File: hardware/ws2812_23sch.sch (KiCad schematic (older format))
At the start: 64 parts

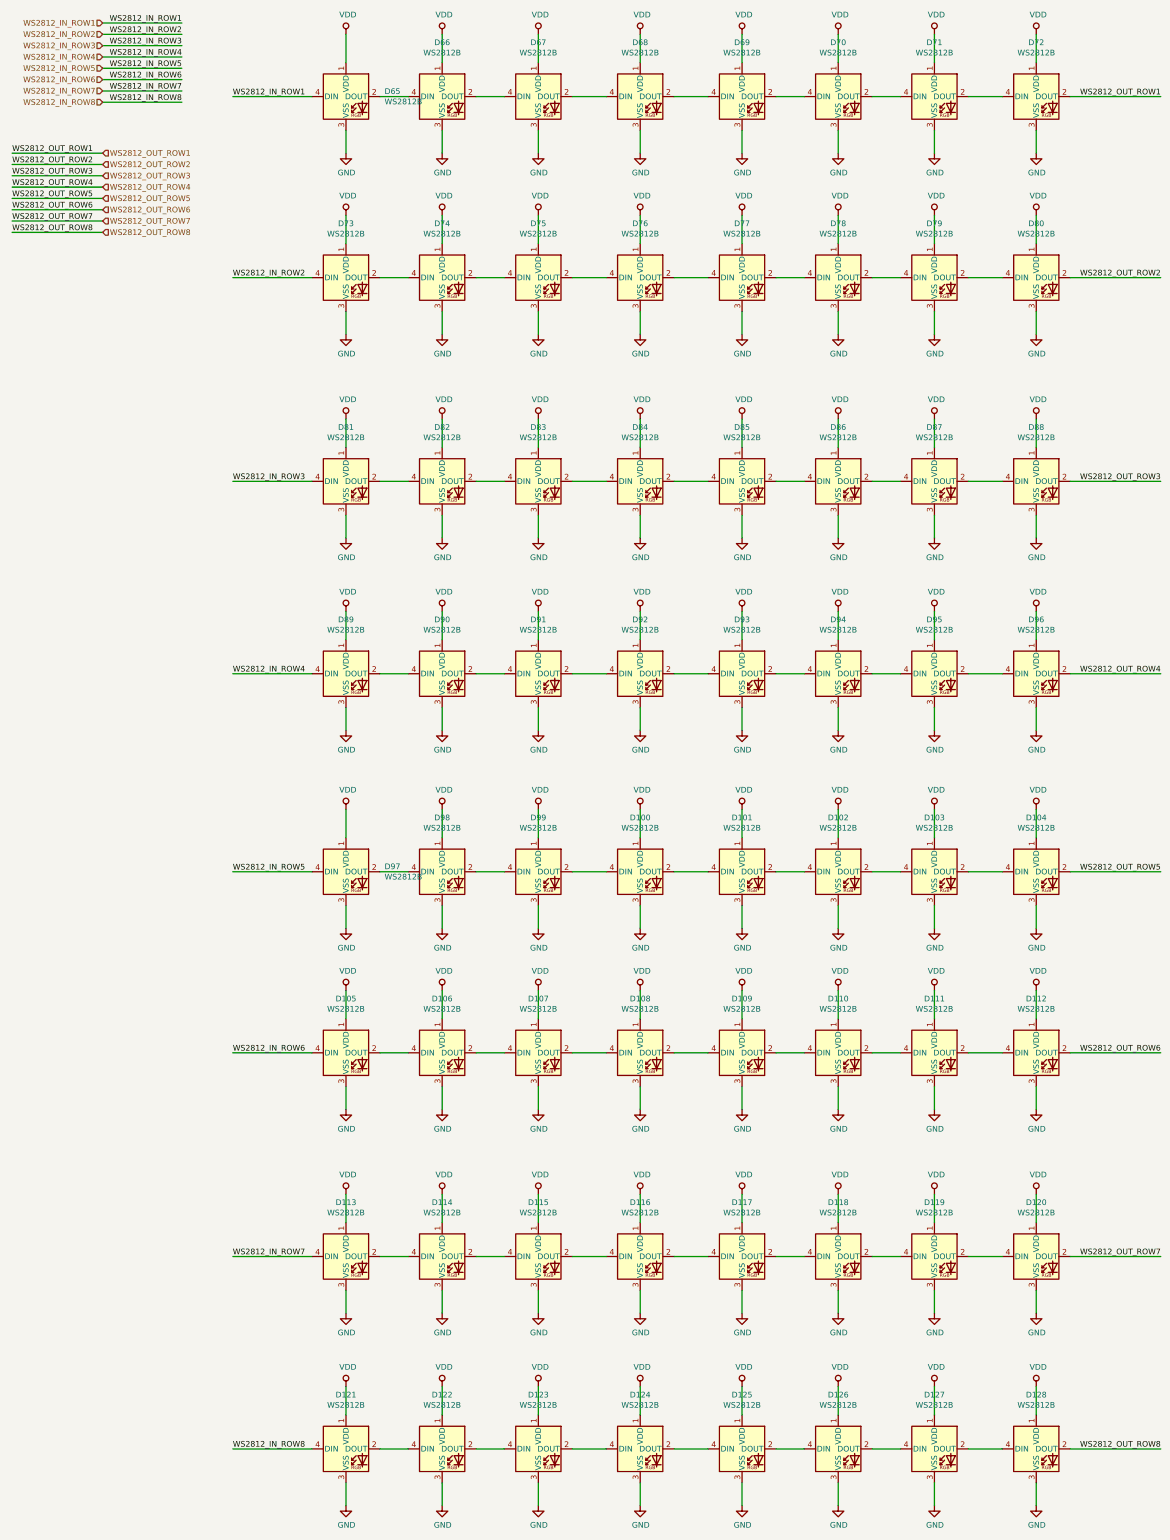
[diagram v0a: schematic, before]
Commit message: update WS2812\,
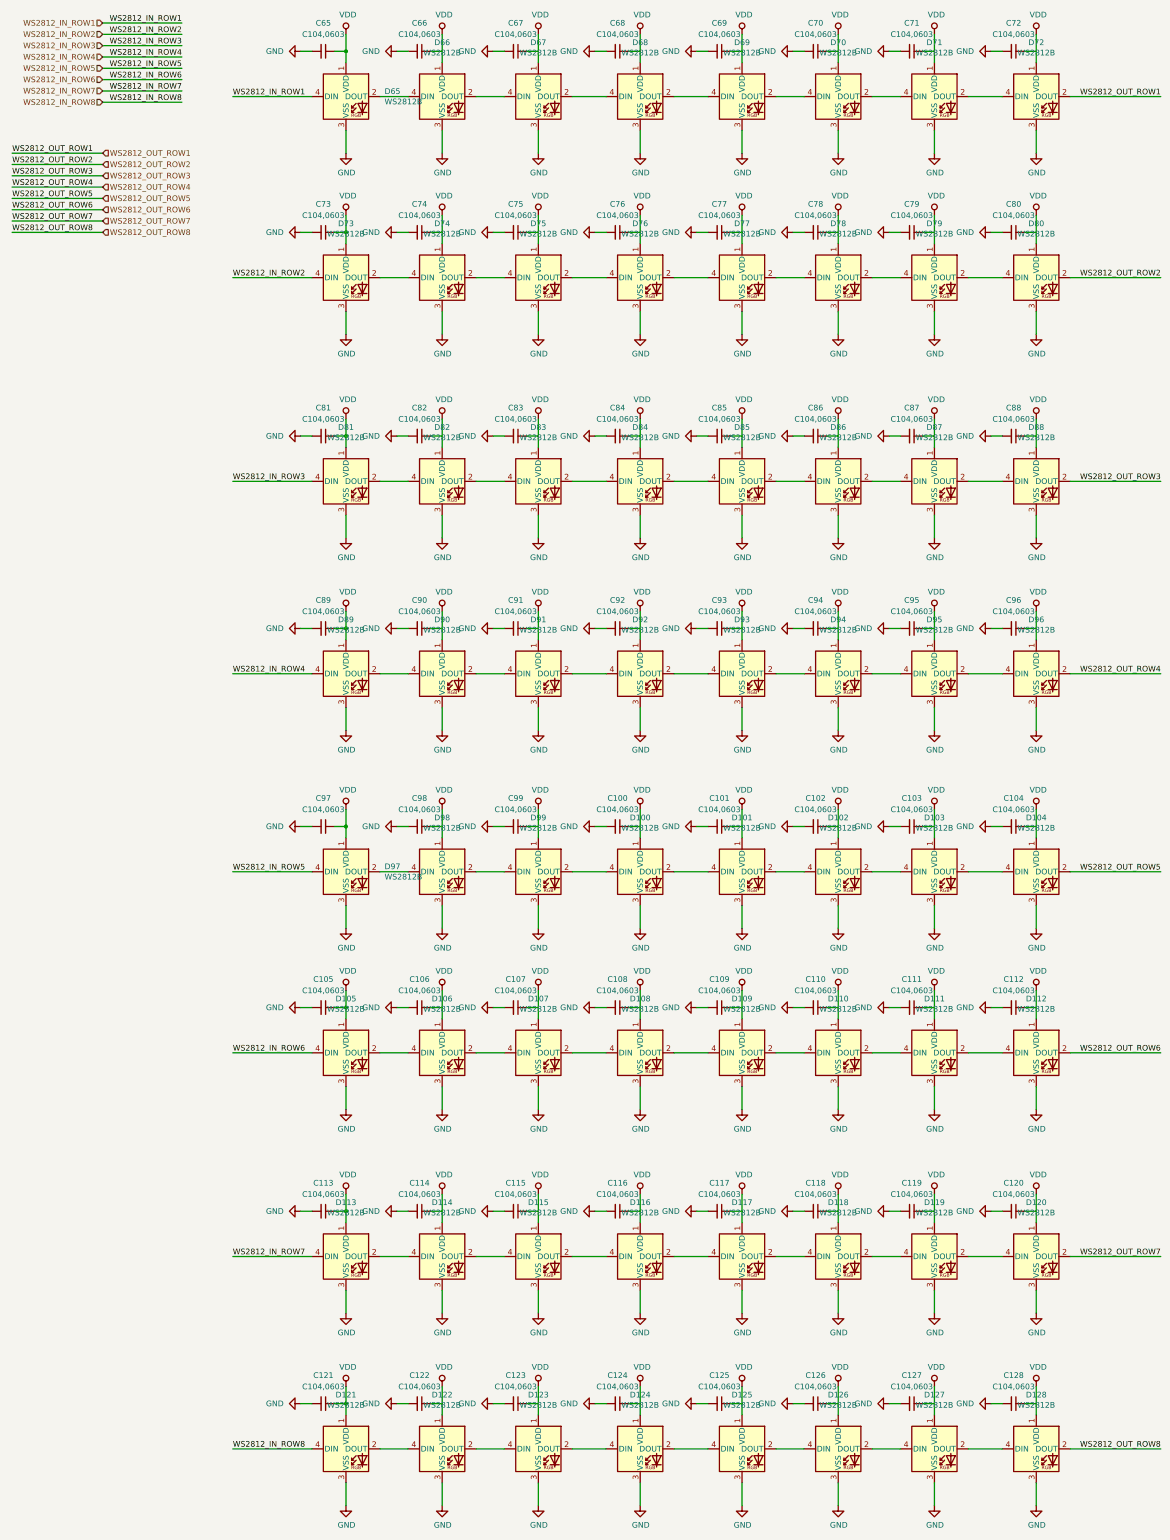
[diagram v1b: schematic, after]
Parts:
- added C100, C101, C102, C103, C104, C105, C106, C107, C108, C109, C110, C111, C112, C113, C114, C115, C116, C117, C118, C119, C120, C121, C122, C123, C124, C125, C126, C127, C128, C65, C66, C67, C68, C69, C70, C71, C72, C73, C74, C75, C76, C77, C78, C79, C80, C81, C82, C83, C84, C85, C86, C87, C88, C89, C90, C91, C92, C93, C94, C95, C96, C97, C98, C99: C104,0603, Capacitor_SMD:C_0603_1608Metric_Pad1.05x0.95mm_HandSolder, symbol taobao-c:C104,0603
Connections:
- wire segments 216 -> 352
